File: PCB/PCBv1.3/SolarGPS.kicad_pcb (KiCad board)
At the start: 2 copper layers, 77 x 32 mm, 55 parts, among them J1 Conn_01x24_Female, J2 Solar1+, J3 GND, J4 Conn_02x03_Odd_Even, J5 Solar2+, J6 GND, J7 Screw_Terminal_01x01, J8 Conn_01x04_Male, Q1 Q_NMOS_GSD, U1 STM32L011G4Ux, U2 MAX-M10Q, U6 LIS3DH, U7 TPS63802, Y1 32.768

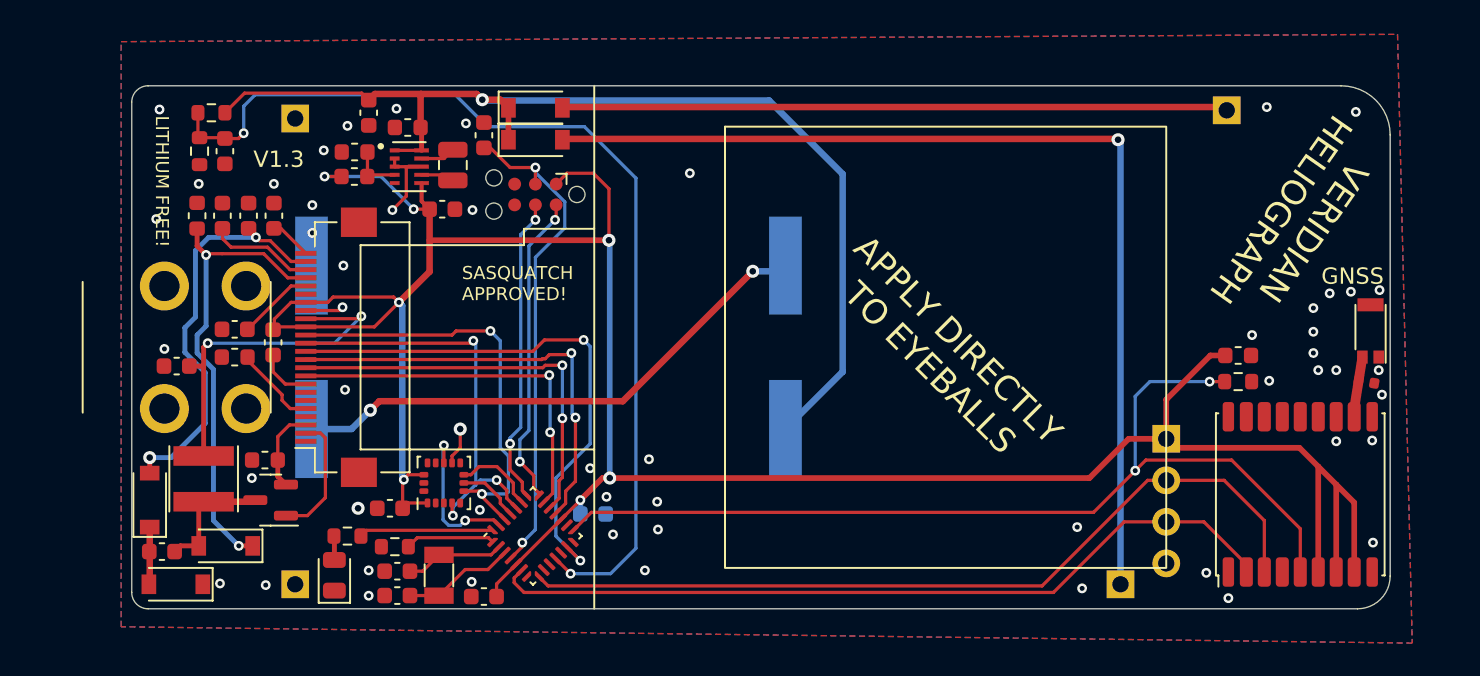
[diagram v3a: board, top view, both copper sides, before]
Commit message: Rework power system for hybrid cap and bq25770
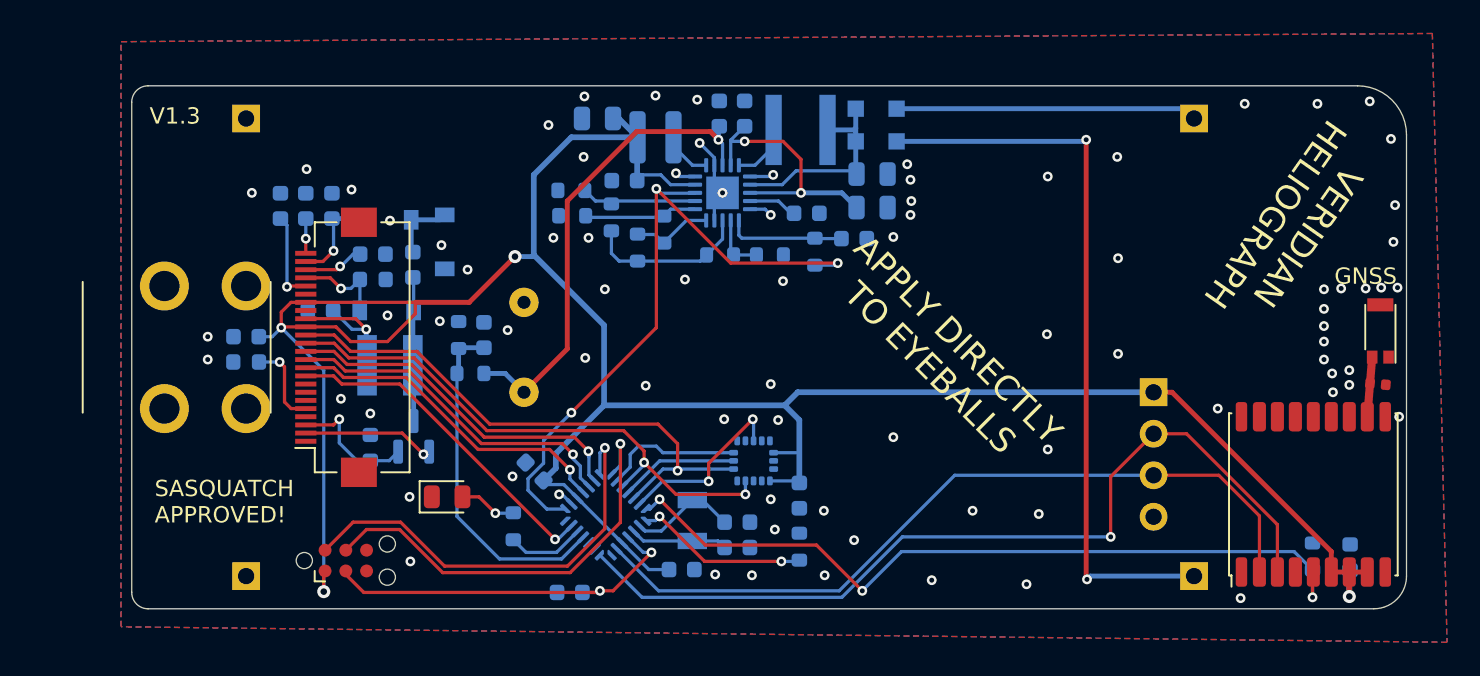
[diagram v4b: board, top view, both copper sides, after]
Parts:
- removed R5: 91k, Resistor_SMD:R_0603_1608Metric
- removed REF**: ER-EPD0154-2R, Heliograph:ER-EPD0154-2R
- removed U7: TPS63802, Heliograph:VREG_TPS63802DLAR
- added C19: 22uF, Capacitor_SMD:C_0805_2012Metric, B.Cu at (78.5, 52.0)
- added C23: 10000pF, Capacitor_SMD:C_0603_1608Metric, B.Cu at (80.2, 55.8)
- added C24: 22uF, Capacitor_SMD:C_0805_2012Metric, B.Cu at (95.3, 57.5)
- added C27: 10000pF, Capacitor_SMD:C_0603_1608Metric, B.Cu at (87.5, 51.7)
- added L3: 10uH, Heliograph:744029100, B.Cu at (82.0, 53.1)
- added ROK1: 3.09M, Resistor_SMD:R_0603_1608Metric, B.Cu at (81.0, 59.9)
- added ROK2: 4.42M, Resistor_SMD:R_0603_1608Metric, B.Cu at (82.5, 58.8)
- added ROK3: 5.36M, Resistor_SMD:R_0603_1608Metric, B.Cu at (77.0, 58.0)
- added ROUT1: 7.87M, Resistor_SMD:R_0603_1608Metric, B.Cu at (79.3, 58.0)
- added ROUT2: 5.36M, Resistor_SMD:R_0603_1608Metric, B.Cu at (76.9, 56.4)
- added ROV1: 6.34M, Resistor_SMD:R_0603_1608Metric, B.Cu at (86.0, 60.4)
- added ROV2: 6.34M, Resistor_SMD:R_0603_1608Metric, B.Cu at (89.0, 60.4)
- added U3: BQ25570, Package_DFN_QFN:QFN-20-1EP_3.5x3.5mm_P0.5mm_EP2x2mm, B.Cu at (86.2, 56.5)
- C10, C13, C15, C16, C18, C2, C20, C21, C22, C25, C26, C3, C4, C5, C6, C9, D4, D5, D6, L1, Q1, R1, R12, R13, R2, R3, R7, U1, U6, Y1: moved to B.Cu
- C12: value 22uF -> 4.7uF; footprint Capacitor_SMD:C_0603_1608Metric -> Capacitor_SMD:C_0805_2012Metric; moved to B.Cu
- C14: value 10F -> 1uF; footprint Heliograph:SCCT20E106SRB_SMD -> Capacitor_SMD:C_0603_1608Metric
- C17: value 10F -> 10000pF; footprint Heliograph:SCCT20E106SRB_SMD -> Capacitor_SMD:C_0603_1608Metric
- C7: value 22uF -> 1uF; moved to B.Cu
- C8: value 1uF -> 30F; footprint Capacitor_SMD:C_0603_1608Metric -> Heliograph:SCCT30E156SRB; moved to B.Cu
- D1, D3: value MBR0530 -> Schottky; footprint Diode_SMD:D_SOD-123 -> Diode_SMD:D_SOD-323_HandSoldering; moved to B.Cu
- J2: value Solar1+ -> GND
- J6: value GND -> Solar1+
- L2: value 0.47uH -> 22uH; footprint Inductor_SMD:L_0806_2016Metric -> Heliograph:744031220; moved to B.Cu
- R4: value 432k -> 1M; moved to B.Cu
- moved J2 66.4 mm to (57.0, 80.0), turned to 180 degrees
- moved J6 61.9 mm to (115.0, 52.0), turned to 180 degrees
- moved C17 31.4 mm to (91.3, 57.8), turned to 180 degrees
- moved C12 31.0 mm to (95.3, 55.4), turned to 180 degrees
- moved R4 28.5 mm to (91.8, 60.1), turned to 90 degrees
- moved C18 28.5 mm to (76.8, 81.0), turned to 0 degrees
- moved D6 26.6 mm to (69.2, 59.5), turned to 90 degrees
- moved J4 25.2 mm to (63.1, 79.0), turned to 0 degrees
- moved C26 25.1 mm to (90.8, 75.1), turned to 90 degrees
- moved R1 24.8 mm to (90.8, 78.2), turned to -90 degrees
- moved L2 23.5 mm to (93.1, 52.7), turned to 180 degrees
- moved C22 23.3 mm to (67.2, 61.0), turned to 90 degrees
- moved R12 22.5 mm to (70.7, 67.6)
- moved D5 22.4 mm to (65.5, 58.2), turned to 180 degrees
- moved C4 21.0 mm to (87.0, 76.7), turned to 0 degrees
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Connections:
- C12 pad 2: VBAT -> /SOLAR+
- C14 pad 1: VBAT -> GND
- C17 pad 1: Net-(C14-Pad2) -> GND
- C17 pad 2: GND -> Net-(C17-Pad2)
- C7 pad 2: VDD -> VBAT
- C8 pad 1: GND -> VBAT
- C8 pad 2: VBAT -> GND
- D1 pad 1: VBAT -> /SOLAR+
- D3 pad 1: VBAT -> /SOLAR+
- J2 pad 1: Net-(D3-Pad2) -> GND
- J6 pad 1: GND -> Net-(D3-Pad2)
- L2 pad 1: Net-(L2-Pad1) -> /SOLAR+
- R4 pad 1: Net-(R4-Pad1) -> VBAT_OK
- R4 pad 2: VDD -> Net-(C14-Pad2)
- U1 pad 12: unconnected-(U1-Pad12) -> LED
- U1 pad 13: DISP_CS -> DISP_BUSY
- U1 pad 15: GPS_EXINT -> VBAT_OK
- U1 pad 18: DISP_DC -> DISP_RES#
- U1 pad 19: DISP_RES# -> DISP_DC
- U1 pad 20: DISP_BUSY -> DISP_CS
- U1 pad 28: LED -> GPS_EXINT
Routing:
- net VBAT_OK: track 0.00 -> 41.4 mm, vias 0 -> 3
- net VBAT_SENSE: track 61.1 -> 21.2 mm, vias 2 -> 0
- net VBAT: track 66.6 -> 29.5 mm
- net Net-(C14-Pad2): track 33.1 -> 7.27 mm, vias 2 -> 0
- net /VGH: track 28.5 -> 5.71 mm, vias 2 -> 1
- net Net-(D3-Pad2): track 40.8 -> 18.4 mm
- net /VGL: track 25.0 -> 5.57 mm, vias 2 -> 1
- net VSTOR: track 0.00 -> 16.5 mm, vias 0 -> 2
- net Net-(D1-Pad2): track 61.2 -> 45.2 mm, vias 1 -> 2
- net /VCI: track 21.8 -> 8.69 mm, vias 2 -> 1
- net GPS_EXINT: track 61.0 -> 48.1 mm, vias 2 -> 3
- net /SOLAR+: track 0.00 -> 12.5 mm
- net DISP_CS: track 33.6 -> 21.8 mm, vias 2 -> 1
- net Net-(ROK1-Pad2): track 0.00 -> 10.1 mm
- net SPI_CLK: track 26.1 -> 34.0 mm, vias 3 -> 2
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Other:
- board size 77 x 32 mm -> 78 x 32 mm
- board text removed: "LITHIUM FREE!"

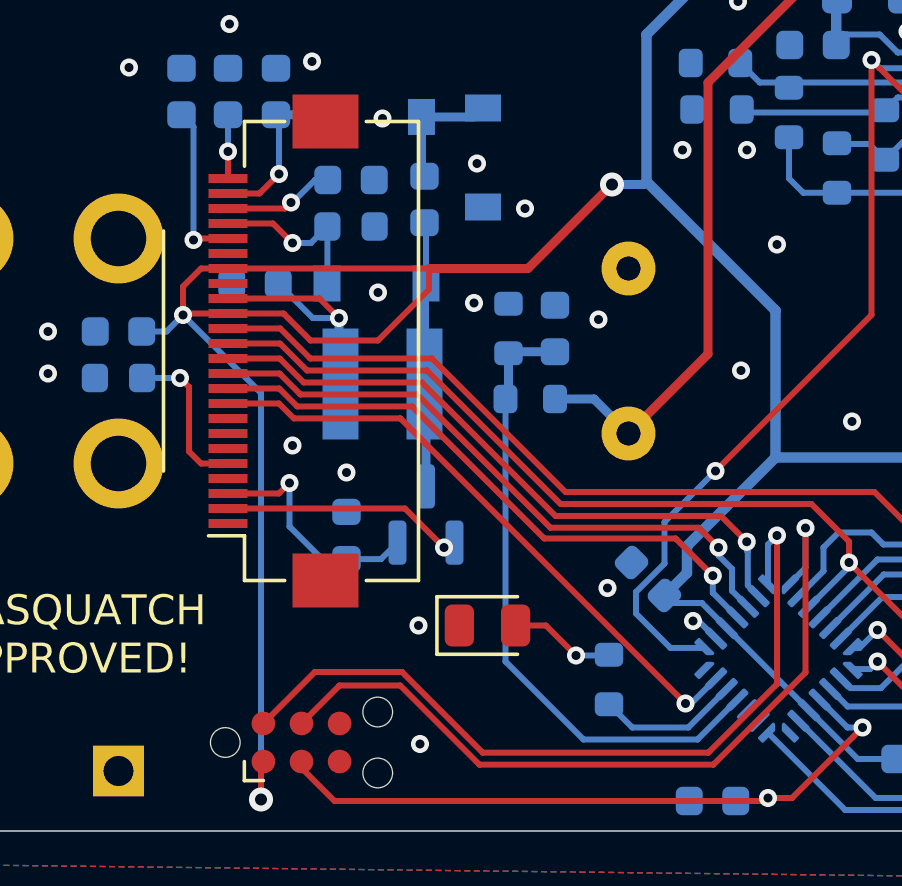
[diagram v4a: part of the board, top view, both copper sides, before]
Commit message: Tweak Epaper driver
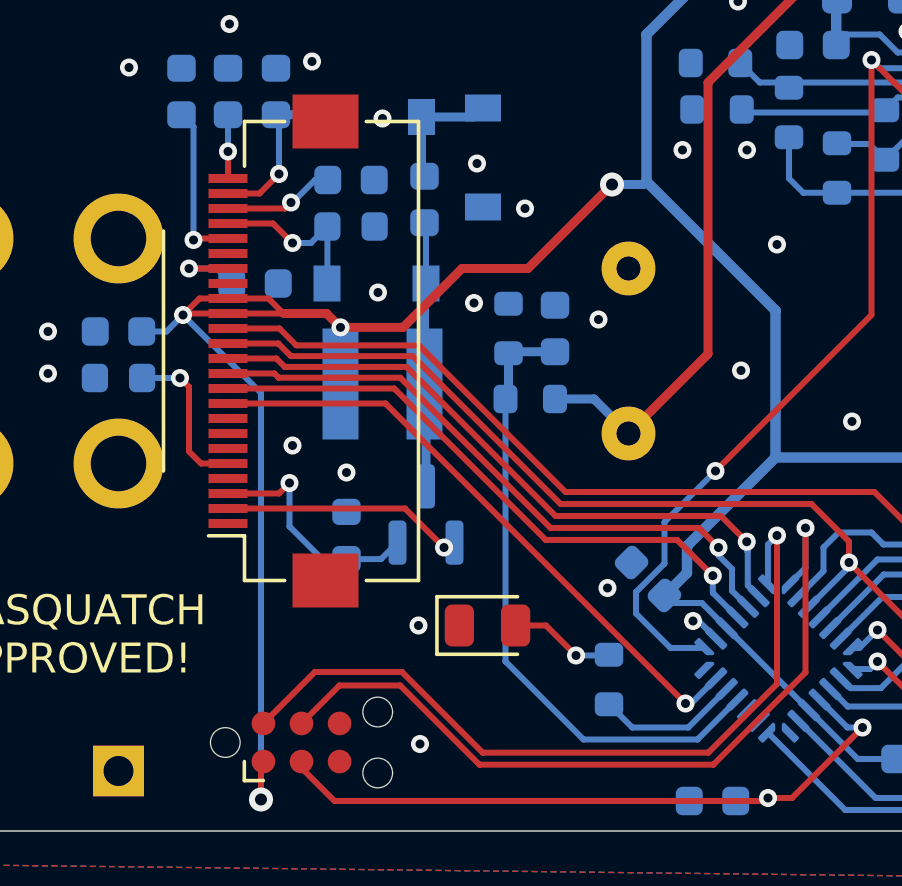
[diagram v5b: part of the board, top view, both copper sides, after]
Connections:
- C16 pad 1: GND -> Net-(C16-Pad1)
- C16 pad 2: /VCI -> GND
- J1 pad 16: /VCI -> VDD
- J1 pad 18: VDD -> Net-(C16-Pad1)
- L1 pad 1: /VCI -> VDD
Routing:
- net /VCI: track 8.69 -> 0.00 mm, vias 1 -> 0
- net VDD: track 159.5 -> 153.1 mm, vias 4 -> 5
- net Net-(C16-Pad1): track 0.00 -> 2.93 mm, vias 0 -> 1

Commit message: Fix Reverse Epaper Connector
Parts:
- J1: footprint Connector_FFC-FPC:Hirose_FH12-24S-0.5SH_1x24-1MP_P0.50mm_Horizontal -> Heliograph:ER-CON24HT-1
- moved C21 17.7 mm to (58.7, 74.7), turned to 90 degrees
- moved C6 17.5 mm to (61.8, 74.7), turned to -90 degrees
- moved C2 17.3 mm to (60.2, 74.7), turned to -90 degrees
- moved C3 16.2 mm to (57.1, 74.7), turned to -90 degrees
- moved R3 15.8 mm to (63.5, 56.4), turned to 180 degrees
- moved Q1 12.8 mm to (64.2, 59.0), turned to 0 degrees
- moved C20 10.6 mm to (65.9, 72.3), turned to -90 degrees
- moved L1 9.88 mm to (68.5, 57.6), turned to -90 degrees
- moved R13 8.09 mm to (68.3, 73.2), turned to 0 degrees
- moved D5 7.29 mm to (64.2, 65.4), turned to -90 degrees
- moved C13 7.13 mm to (68.3, 71.6), turned to 0 degrees
- moved D6 6.40 mm to (66.5, 65.4)
- moved C16 5.48 mm to (57.0, 66.8), turned to 180 degrees
- moved C15 5.15 mm to (62.1, 65.3), turned to -90 degrees
- moved R12 4.85 mm to (70.7, 72.5), turned to 90 degrees
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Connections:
- U1 pad 13: DISP_BUSY -> unconnected-(U1-Pad13)
- U1 pad 14: unconnected-(U1-Pad14) -> DISP_BUSY
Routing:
- net DISP_RES#: track 20.5 -> 33.2 mm
- net DISP_DC: track 21.1 -> 29.8 mm
- net /VGL: track 5.57 -> 12.4 mm, vias 1 -> 2
- net /SWDCLK: track 26.6 -> 19.9 mm
- net /VGH: track 5.71 -> 12.2 mm
- net /SWDIO: track 26.6 -> 20.6 mm
- net VBAT_SENSE: track 21.2 -> 16.3 mm
- net /GDR: track 8.16 -> 3.48 mm
- net VBAT: track 29.5 -> 33.7 mm
- net DISP_CS: track 21.8 -> 25.8 mm
- net VBAT_OK: track 41.4 -> 45.1 mm
- net DISP_BUSY: track 20.8 -> 24.2 mm
- net SPI_CLK: track 34.0 -> 37.2 mm
- net /RESE: track 7.92 -> 10.4 mm
- net /VSL: track 3.57 -> 5.57 mm
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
